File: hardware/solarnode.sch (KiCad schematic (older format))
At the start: 32 parts, among them IC1 STM32F0xxFxPx, P1 USB_OTG, P2 TC2030-CTX, P3 C_PANEL, P4 C_BATT, U2 CN3083, U3 MCP1700, U4 RFM69HW, U5 DS18B20, U6 DS18B20

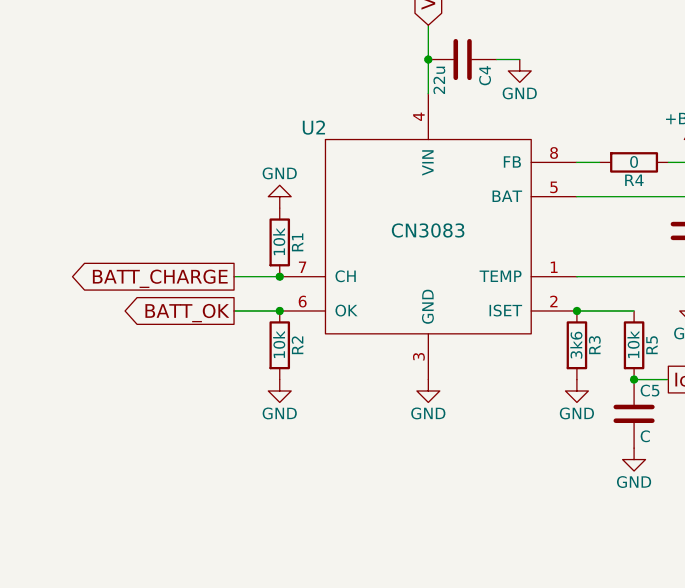
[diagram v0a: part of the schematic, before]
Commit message: Fix open-drain pull-ups to be actual pull-ups
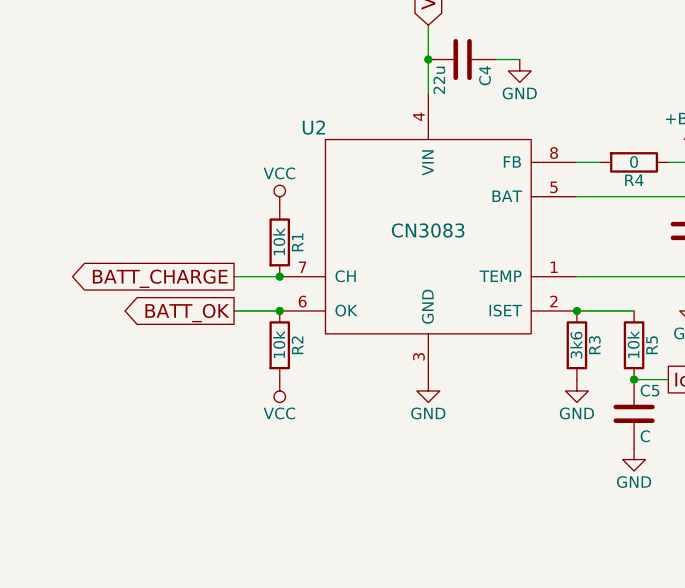
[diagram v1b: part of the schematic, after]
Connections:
- net GND: no longer R1.1, R2.2
- net VCC: now also R1.1, R2.2
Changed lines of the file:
@@
 	3650 5900 3450 5900
-$Comp
-L GND #PWR027
-U 1 1 5710F1DE
-P 3650 6200
-F 0 "#PWR027" H 3650 5950 50  0001 C CNN
-F 1 "GND" H 3650 6050 50  0000 C CNN
-F 2 "" H 3650 6200 50  0000 C CNN
-F 3 "" H 3650 6200 50  0000 C CNN
-	1    3650 6200
-	1    0    0    -1
-$EndComp
-$Comp
-L GND #PWR028
-U 1 1 5710F246
-P 3650 5450
-F 0 "#PWR028" H 3650 5200 50  0001 C CNN
-F 1 "GND" H 3650 5300 50  0000 C CNN
-F 2 "" H 3650 5450 50  0000 C CNN
-F 3 "" H 3650 5450 50  0000 C CNN
-	1    3650 5450
-	-1   0    0    1
-$EndComp
 $Comp
 L Jumper_NO_Small JP1
@@
 $EndComp
 Connection ~ 6550 2900
+$Comp
+L VCC #PWR?
+U 1 1 5713D184
+P 3650 5450
+F 0 "#PWR?" H 3650 5300 50  0001 C CNN
+F 1 "VCC" H 3650 5600 50  0000 C CNN
+F 2 "" H 3650 5450 50  0000 C CNN
+F 3 "" H 3650 5450 50  0000 C CNN
+	1    3650 5450
+	1    0    0    -1
+$EndComp
+$Comp
+L VCC #PWR?
+U 1 1 5713D318
+P 3650 6200
+F 0 "#PWR?" H 3650 6050 50  0001 C CNN
+F 1 "VCC" H 3650 6350 50  0000 C CNN
+F 2 "" H 3650 6200 50  0000 C CNN
+F 3 "" H 3650 6200 50  0000 C CNN
+	1    3650 6200
+	-1   0    0    1
+$EndComp
 $EndSCHEMATC

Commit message: Version 1.1
- Fix incorrect RFM69 SPI wiring
- Remove unneeded pullup resistors on CN3083 open-drain outputs
- Fix silk text sizing so it's actually readable
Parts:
- removed R1, R2: 10k, Resistors_SMD:R_0805, symbol R
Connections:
- net at U4.2 (NSS): now also IC1.10 (PA4); no longer IC1.9 (PA3)
- net at U4.3 (MOSI): now also IC1.13 (PA7); no longer IC1.12 (PA6)
- net at U4.4 (MISO): now also IC1.12 (PA6); no longer IC1.11 (PA5)
- net at U4.5 (SCK): now also IC1.11 (PA5); no longer IC1.10 (PA4)
- net RFM_RST: now reaches U4.9 (RESET)
- net RFM_RST: now also IC1.9 (PA3); no longer IC1.13 (PA7)
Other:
- moved on the sheet: ANT1, C8, U4
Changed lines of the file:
@@
 Sheet 1 1
 Title "UKHASnet Solar Node"
-Date "15/04/2016"
-Rev "1"
+Date "20/05/2016"
+Rev "1.1"
 Comp "Russ Garrett"
 Comment1 ""
@@
 L RFM69HW U4
 U 1 1 570EA289
-P 6550 2300
-F 0 "U4" H 6200 2850 60  0000 C CNN
-F 1 "RFM69HW" H 6850 1800 60  0000 C CNN
-F 2 "tinkerforge:RFM69HW" H 6200 2850 60  0001 C CNN
-F 3 "" H 6200 2850 60  0000 C CNN
-	1    6550 2300
+P 6550 2400
+F 0 "U4" H 6200 2950 60  0000 C CNN
+F 1 "RFM69HW" H 6850 1900 60  0000 C CNN
+F 2 "tinkerforge:RFM69HW" H 6200 2950 60  0001 C CNN
+F 3 "" H 6200 2950 60  0000 C CNN
+	1    6550 2400
 	1    0    0    -1
 $EndComp
@@
 L GND #PWR03
 U 1 1 570EA34F
-P 6550 2900
-F 0 "#PWR03" H 6550 2650 50  0001 C CNN
-F 1 "GND" H 6550 2750 50  0000 C CNN
-F 2 "" H 6550 2900 50  0000 C CNN
-F 3 "" H 6550 2900 50  0000 C CNN
-	1    6550 2900
+P 6550 3000
+F 0 "#PWR03" H 6550 2750 50  0001 C CNN
+F 1 "GND" H 6550 2850 50  0000 C CNN
+F 2 "" H 6550 3000 50  0000 C CNN
+F 3 "" H 6550 3000 50  0000 C CNN
+	1    6550 3000
 	1    0    0    -1
 $EndComp
@@
 L VCC #PWR04
 U 1 1 570EA369
-P 6550 1700
-F 0 "#PWR04" H 6550 1550 50  0001 C CNN
-F 1 "VCC" H 6550 1850 50  0000 C CNN
-F 2 "" H 6550 1700 50  0000 C CNN
-F 3 "" H 6550 1700 50  0000 C CNN
-	1    6550 1700
+P 6550 1800
+F 0 "#PWR04" H 6550 1650 50  0001 C CNN
+F 1 "VCC" H 6550 1950 50  0000 C CNN
+F 2 "" H 6550 1800 50  0000 C CNN
+F 3 "" H 6550 1800 50  0000 C CNN
+	1    6550 1800
 	1    0    0    -1
 $EndComp
@@
 L CON-SMA ANT1
 U 1 1 570EBF25
-P 7800 2950
-F 0 "ANT1" H 7700 3500 60  0000 C CNN
-F 1 "ANT" V 8050 3150 60  0000 C CNN
-F 2 "tinkerforge:CON-SMA-EDGE" H 7800 2950 60  0001 C CNN
-F 3 "" H 7800 2950 60  0000 C CNN
-	1    7800 2950
+P 7800 3050
+F 0 "ANT1" H 7700 3600 60  0000 C CNN
+F 1 "ANT" V 8050 3250 60  0000 C CNN
+F 2 "tinkerforge:CON-SMA-EDGE" H 7800 3050 60  0001 C CNN
+F 3 "" H 7800 3050 60  0000 C CNN
+	1    7800 3050
 	1    0    0    -1
 $EndComp
@@
 L GND #PWR05
 U 1 1 570EBFA2
-P 7800 3200
-F 0 "#PWR05" H 7800 2950 50  0001 C CNN
-F 1 "GND" H 7800 3050 50  0000 C CNN
-F 2 "" H 7800 3200 50  0000 C CNN
-F 3 "" H 7800 3200 50  0000 C CNN
-	1    7800 3200
+P 7800 3300
+F 0 "#PWR05" H 7800 3050 50  0001 C CNN
+F 1 "GND" H 7800 3150 50  0000 C CNN
+F 2 "" H 7800 3300 50  0000 C CNN
+F 3 "" H 7800 3300 50  0000 C CNN
+	1    7800 3300
 	1    0    0    -1
 $EndComp
@@
 $EndComp
 NoConn ~ 10150 3850
-NoConn ~ 7100 2450
+NoConn ~ 7100 2550
+NoConn ~ 7100 2350
 NoConn ~ 7100 2250
 NoConn ~ 7100 2150
-NoConn ~ 7100 2050
-NoConn ~ 6000 1950
+NoConn ~ 6000 2050
 NoConn ~ 5600 3350
 NoConn ~ 9200 8250
 Wire Wire Line
-	6500 2900 6600 2900
-Connection ~ 6600 2900
-Connection ~ 6500 2900
-Wire Wire Line
-	5000 2350 5450 2350
-Wire Wire Line
-	5450 2350 5450 2450
-Wire Wire Line
-	5450 2450 6000 2450
-Wire Wire Line
-	5000 2450 5350 2450
-Wire Wire Line
-	5350 2450 5350 2400
-Wire Wire Line
-	5350 2400 5650 2400
-Wire Wire Line
-	5650 2400 5650 2350
-Wire Wire Line
-	5650 2350 6000 2350
-Wire Wire Line
-	6000 2250 5000 2250
-Wire Wire Line
-	5000 2150 6000 2150
-Wire Wire Line
-	6000 2650 6000 2550
-Wire Wire Line
-	6000 2550 5000 2550
-Wire Wire Line
-	7100 2650 7450 2650
-Wire Wire Line
-	7650 3200 7950 3200
-Connection ~ 7650 3200
-Connection ~ 7750 3200
-Connection ~ 7850 3200
-Connection ~ 7950 3200
+	6500 3000 6600 3000
+Connection ~ 6600 3000
+Connection ~ 6500 3000
+Wire Wire Line
+	5450 2550 6000 2550
+Wire Wire Line
+	5000 2550 5400 2550
+Wire Wire Line
+	5500 2450 6000 2450
+Wire Wire Line
+	6000 2350 5000 2350
+Wire Wire Line
+	5000 2250 6000 2250
+Wire Wire Line
+	7100 2750 7450 2750
+Wire Wire Line
+	7650 3300 7950 3300
+Connection ~ 7650 3300
+Connection ~ 7750 3300
+Connection ~ 7850 3300
+Connection ~ 7950 3300
 Wire Wire Line
 	5000 2750 5800 2750
@@
 Connection ~ 9500 5500
 Connection ~ 9500 5300
-Connection ~ 7800 3200
+Connection ~ 7800 3300
 $Comp
 L R R8
@@
 L C_Small C8
 U 1 1 5710DE1F
-P 6750 1700
-F 0 "C8" H 6760 1770 50  0000 L CNN
-F 1 "100n" H 6760 1620 50  0000 L CNN
-F 2 "Capacitors_SMD:C_0805" H 6750 1700 50  0001 C CNN
-F 3 "" H 6750 1700 50  0000 C CNN
-	1    6750 1700
+P 6750 1800
+F 0 "C8" H 6760 1870 50  0000 L CNN
+F 1 "100n" H 6760 1720 50  0000 L CNN
+F 2 "Capacitors_SMD:C_0805" H 6750 1800 50  0001 C CNN
+F 3 "" H 6750 1800 50  0000 C CNN
+	1    6750 1800
 	0    -1   -1   0
 $EndComp
 Wire Wire Line
-	6650 1700 6550 1700
-Connection ~ 6550 1700
+	6650 1800 6550 1800
+Connection ~ 6550 1800
 $Comp
 L GND #PWR025
 U 1 1 5710DF88
-P 6850 1700
-F 0 "#PWR025" H 6850 1450 50  0001 C CNN
-F 1 "GND" H 6850 1550 50  0000 C CNN
-F 2 "" H 6850 1700 50  0000 C CNN
-F 3 "" H 6850 1700 50  0000 C CNN
-	1    6850 1700
+P 6850 1800
+F 0 "#PWR025" H 6850 1550 50  0001 C CNN
+F 1 "GND" H 6850 1650 50  0000 C CNN
+F 2 "" H 6850 1800 50  0000 C CNN
+F 3 "" H 6850 1800 50  0000 C CNN
+	1    6850 1800
 	0    -1   -1   0
 $EndComp
@@
 Text GLabel 3800 2850 0    60   Input ~ 0
 BATT_OK
-$Comp
-L R R1
-U 1 1 5710EFC9
-P 3650 5600
-F 0 "R1" V 3730 5600 50  0000 C CNN
-F 1 "10k" V 3650 5600 50  0000 C CNN
-F 2 "Resistors_SMD:R_0805" V 3580 5600 50  0001 C CNN
-F 3 "" H 3650 5600 50  0000 C CNN
-	1    3650 5600
-	1    0    0    -1
-$EndComp
-$Comp
-L R R2
-U 1 1 5710F032
-P 3650 6050
-F 0 "R2" V 3730 6050 50  0000 C CNN
-F 1 "10k" V 3650 6050 50  0000 C CNN
-F 2 "Resistors_SMD:R_0805" V 3580 6050 50  0001 C CNN
-F 3 "" H 3650 6050 50  0000 C CNN
-	1    3650 6050
-	1    0    0    -1
-$EndComp
 Text GLabel 3450 5750 0    60   Output ~ 0
 BATT_CHARGE
@@
 Wire Wire Line
 	10200 5400 10500 5400
-$Comp
-L CN3083 U2
-U 1 1 57110BE8
-P 4300 5650
-F 0 "U2" H 3800 6200 60  0000 C CNN
-F 1 "CN3083" H 4300 5750 60  0000 C CNN
-F 2 "agg:SOIC-8-EP-CN" H 4300 5750 60  0001 C CNN
-F 3 "" H 4300 5750 60  0000 C CNN
-	1    4300 5650
-	1    0    0    -1
-$EndComp
-Connection ~ 3650 5750
-Connection ~ 3650 5900
 Wire Wire Line
 	3800 2550 3000 2550
@@
 Wire Wire Line
 	3800 2050 3600 2050
-NoConn ~ 7100 2350
-NoConn ~ 7100 1950
+NoConn ~ 7100 2450
+NoConn ~ 7100 2050
 $Comp
 L C C6
@@
 	1    0    0    -1
 $EndComp
-Connection ~ 6550 2900
-$Comp
-L VCC #PWR?
-U 1 1 5713D184
-P 3650 5450
-F 0 "#PWR?" H 3650 5300 50  0001 C CNN
-F 1 "VCC" H 3650 5600 50  0000 C CNN
-F 2 "" H 3650 5450 50  0000 C CNN
-F 3 "" H 3650 5450 50  0000 C CNN
-	1    3650 5450
-	1    0    0    -1
-$EndComp
-$Comp
-L VCC #PWR?
-U 1 1 5713D318
-P 3650 6200
-F 0 "#PWR?" H 3650 6050 50  0001 C CNN
-F 1 "VCC" H 3650 6350 50  0000 C CNN
-F 2 "" H 3650 6200 50  0000 C CNN
-F 3 "" H 3650 6200 50  0000 C CNN
-	1    3650 6200
-	-1   0    0    1
-$EndComp
+Connection ~ 6550 3000
+Wire Wire Line
+	5450 2550 5450 2450
+Wire Wire Line
+	5450 2450 5000 2450
+Wire Wire Line
+	5400 2550 5400 2500
+Wire Wire Line
+	5400 2500 5500 2500
+Wire Wire Line
+	5500 2500 5500 2450
+Text GLabel 6000 2650 0    60   Input ~ 0
+RFM_RST
+Wire Wire Line
+	6000 2650 6000 2750
+Text GLabel 5000 2150 2    60   Output ~ 0
+RFM_RST
+$Comp
+L CN3083 U2
+U 1 1 57110BE8
+P 4300 5650
+F 0 "U2" H 3800 6200 60  0000 C CNN
+F 1 "CN3083" H 4300 5750 60  0000 C CNN
+F 2 "agg:SOIC-8-EP-CN" H 4300 5750 60  0001 C CNN
+F 3 "" H 4300 5750 60  0000 C CNN
+	1    4300 5650
+	1    0    0    -1
+$EndComp
+Connection ~ 5300 3750
 $EndSCHEMATC

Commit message: Remove unneeded boot jumper
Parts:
- removed JP1: Boot, Resistors_SMD:R_0805, symbol Jumper_NO_Small
- IC1: value STM32F0xxFxPx -> STM32F042F6P6
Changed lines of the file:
@@
 	3650 5900 3450 5900
 $Comp
-L Jumper_NO_Small JP1
-U 1 1 5710F5F9
-P 2900 2800
-F 0 "JP1" H 2900 2880 50  0000 C CNN
-F 1 "Boot" H 2910 2740 50  0001 C CNN
-F 2 "Resistors_SMD:R_0805" H 2900 2800 50  0001 C CNN
-F 3 "" H 2900 2800 50  0000 C CNN
-	1    2900 2800
-	1    0    0    -1
-$EndComp
-$Comp
-L Led_Small D1
-U 1 1 5710F743
-P 2900 2550
-F 0 "D1" H 2850 2675 50  0000 L CNN
-F 1 "Status" H 2725 2450 50  0000 L CNN
-F 2 "agg:0805-LED" V 2900 2550 50  0001 C CNN
-F 3 "" V 2900 2550 50  0000 C CNN
-	1    2900 2550
-	1    0    0    -1
-$EndComp
-$Comp
-L GND #PWR029
+L GND #PWR027
 U 1 1 5710F92A
 P 2600 2550
-F 0 "#PWR029" H 2600 2300 50  0001 C CNN
+F 0 "#PWR027" H 2600 2300 50  0001 C CNN
 F 1 "GND" H 2600 2400 50  0000 C CNN
 F 2 "" H 2600 2550 50  0000 C CNN
@@
 $EndComp
 $Comp
-L VCC #PWR030
+L VCC #PWR028
 U 1 1 57110112
 P 9800 1600
-F 0 "#PWR030" H 9800 1450 50  0001 C CNN
+F 0 "#PWR028" H 9800 1450 50  0001 C CNN
 F 1 "VCC" H 9800 1750 50  0000 C CNN
 F 2 "" H 9800 1600 50  0000 C CNN
@@
 $EndComp
 $Comp
-L VCC #PWR031
+L VCC #PWR029
 U 1 1 57110166
 P 9800 2200
-F 0 "#PWR031" H 9800 2050 50  0001 C CNN
+F 0 "#PWR029" H 9800 2050 50  0001 C CNN
 F 1 "VCC" H 9800 2350 50  0000 C CNN
 F 2 "" H 9800 2200 50  0000 C CNN
@@
 $EndComp
 $Comp
-L GND #PWR032
+L GND #PWR030
 U 1 1 571101BA
 P 9800 1800
-F 0 "#PWR032" H 9800 1550 50  0001 C CNN
+F 0 "#PWR030" H 9800 1550 50  0001 C CNN
 F 1 "GND" H 9800 1650 50  0000 C CNN
 F 2 "" H 9800 1800 50  0000 C CNN
@@
 $EndComp
 $Comp
-L GND #PWR033
+L GND #PWR031
 U 1 1 57110282
 P 9800 2400
-F 0 "#PWR033" H 9800 2150 50  0001 C CNN
+F 0 "#PWR031" H 9800 2150 50  0001 C CNN
 F 1 "GND" H 9800 2250 50  0000 C CNN
 F 2 "" H 9800 2400 50  0000 C CNN
@@
 	9500 2300 9800 2300
 $Comp
-L PWR_FLAG #FLG034
+L PWR_FLAG #FLG032
 U 1 1 57110FA7
 P 10500 5500
-F 0 "#FLG034" H 10500 5595 50  0001 C CNN
+F 0 "#FLG032" H 10500 5595 50  0001 C CNN
 F 1 "PWR_FLAG" H 10500 5680 50  0000 C CNN
 F 2 "" H 10500 5500 50  0000 C CNN
@@
 	3800 2550 3000 2550
 Wire Wire Line
-	3000 2550 3000 2800
-Wire Wire Line
-	2800 2800 2800 2550
-Wire Wire Line
 	2800 2550 2600 2550
 Wire Wire Line
@@
 	3800 1850 3600 1850
 $Comp
-L GND #PWR035
+L GND #PWR033
 U 1 1 57112AC9
 P 3600 2050
-F 0 "#PWR035" H 3600 1800 50  0001 C CNN
+F 0 "#PWR033" H 3600 1800 50  0001 C CNN
 F 1 "GND" H 3600 1900 50  0000 C CNN
 F 2 "" H 3600 2050 50  0000 C CNN
@@
 	5450 5700 5450 5850
 Connection ~ 5450 5750
-Connection ~ 3000 2550
-Connection ~ 2800 2550
 Connection ~ 3800 1850
 $Comp
@@
 P 4400 2450
 F 0 "IC1" H 3900 3150 50  0000 L CNN
-F 1 "STM32F0xxFxPx" H 3900 1750 50  0000 L CNN
+F 1 "STM32F042F6P6" H 3900 1750 50  0000 L CNN
 F 2 "tinkerforge:TSSOP20" H 3900 1650 50  0001 L CNN
 F 3 "http://www.st.com/st-web-ui/static/active/en/resource/technical/document/datasheet/DM00105814.pdf" H 3900 1550 50  0001 L CNN
@@
 $EndComp
 Connection ~ 5300 3750
+$Comp
+L Led_Small D1
+U 1 1 5710F743
+P 2900 2550
+F 0 "D1" H 2850 2675 50  0000 L CNN
+F 1 "Status" H 2725 2450 50  0000 L CNN
+F 2 "agg:0805-LED" V 2900 2550 50  0001 C CNN
+F 3 "" V 2900 2550 50  0000 C CNN
+	1    2900 2550
+	1    0    0    -1
+$EndComp
 $EndSCHEMATC
